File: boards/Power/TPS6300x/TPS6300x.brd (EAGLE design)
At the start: 26.7 x 10.2 mm, 9 parts

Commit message: Minor edits to the TPS6300x board and its library footprint
- Added external enable pin (might want this for APRS 3.3v)
- Fixed text issues with the footprint (didn't add EN yet)
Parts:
- added EXT_EN: M01PTH, SparkFun-Connectors:1X01
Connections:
- net EN: now also EXT_EN.1
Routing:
- net EN: track 20.1 -> 25.0 mm
- net 1.8V: track 30.7 -> 32.2 mm
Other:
- board text added: "EN"
- board text added: "v2"
- board text removed: "v1"
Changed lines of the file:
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@@
 <wire x1="26.67" y1="10.16" x2="0" y2="10.16" width="0" layer="20"/>
 <wire x1="0" y1="10.16" x2="0" y2="0" width="0" layer="20"/>
-<text x="23.495" y="0.635" size="1.778" layer="21">-</text>
 <text x="23.495" y="7.62" size="1.778" layer="21">+</text>
 <text x="8.255" y="7.62" size="1.778" layer="21">+</text>
 <text x="9.525" y="7.62" size="1.778" layer="22" rot="MR0">+</text>
 <text x="24.765" y="7.62" size="1.778" layer="22" rot="MR0">+</text>
-<text x="24.765" y="0.635" size="1.778" layer="22" rot="MR0">-</text>
 <text x="9.525" y="0.635" size="1.778" layer="22" rot="MR0">-</text>
-<text x="10.16" y="1.905" size="1.6764" layer="22" rot="MR180">TPS6300x</text>
-<text x="0" y="1.905" size="1.6764" layer="22" rot="MR180">v1</text>
+<text x="10.541" y="9.779" size="1.6764" layer="22" rot="MR180">TPS6300x</text>
+<text x="10.541" y="7.239" size="1.6764" layer="22" rot="MR180">v2</text>
+<text x="22.86" y="1.905" size="1.27" layer="25" rot="R180">EN</text>
 </plain>
 <attributes>
@@
 <attribute name="VALUE" x="3.81" y="0.127" size="0.4064" layer="27"/>
 </element>
+<element name="EXT_EN" library="SparkFun-Connectors" package="1X01" value="M01PTH" x="24.13" y="1.27" smashed="yes"/>
 </elements>
 <signals>
@@
 <wire x1="19.2786" y1="5.715" x2="19.5072" y2="5.4864" width="0.254" layer="1"/>
 <wire x1="19.5072" y1="5.4864" x2="20.5232" y2="4.4704" width="0.4064" layer="1"/>
-<wire x1="20.5232" y1="4.4704" x2="20.5232" y2="2.032" width="0.4064" layer="1"/>
-<wire x1="20.5232" y1="2.032" x2="19.9136" y2="1.4224" width="0.4064" layer="1"/>
-<wire x1="19.9136" y1="1.4224" x2="16.0528" y2="1.4224" width="0.4064" layer="1"/>
-<wire x1="16.0528" y1="1.4224" x2="14.9352" y2="2.54" width="0.4064" layer="1"/>
+<wire x1="20.5232" y1="4.4704" x2="20.5232" y2="3.048" width="0.4064" layer="1"/>
+<wire x1="20.5232" y1="3.048" x2="20.9296" y2="2.6416" width="0.4064" layer="1"/>
+<wire x1="20.9296" y1="2.6416" x2="20.9296" y2="1.4224" width="0.4064" layer="1"/>
+<wire x1="20.9296" y1="1.4224" x2="20.32" y2="0.8128" width="0.4064" layer="1"/>
+<wire x1="20.32" y1="0.8128" x2="16.6624" y2="0.8128" width="0.4064" layer="1"/>
+<wire x1="16.6624" y1="0.8128" x2="14.9352" y2="2.54" width="0.4064" layer="1"/>
 <wire x1="14.9352" y1="2.54" x2="14.875" y2="2.54" width="0.4064" layer="1"/>
 <wire x1="18.62" y1="5.215" x2="19.2358" y2="5.215" width="0.254" layer="1"/>
@@
 <wire x1="4.71" y1="1.27" x2="6.35" y2="1.27" width="0.254" layer="1"/>
 <via x="6.35" y="1.27" extent="1-16" drill="0.6"/>
-<wire x1="6.35" y1="1.27" x2="18.9484" y2="1.27" width="0.254" layer="16"/>
+<wire x1="6.35" y1="1.27" x2="19.1516" y2="1.27" width="0.254" layer="16"/>
 <wire x1="18.62" y1="4.715" x2="18.8562" y2="4.715" width="0.254" layer="1"/>
-<wire x1="18.8562" y1="4.715" x2="19.5072" y2="4.064" width="0.254" layer="1"/>
-<wire x1="19.5072" y1="4.064" x2="19.5072" y2="3.8608" width="0.254" layer="1"/>
-<via x="19.5072" y="3.8608" extent="1-16" drill="0.6"/>
-<wire x1="19.5072" y1="3.8608" x2="19.5072" y2="1.8288" width="0.254" layer="16"/>
-<wire x1="19.5072" y1="1.8288" x2="18.9484" y2="1.27" width="0.254" layer="16"/>
+<wire x1="18.8562" y1="4.715" x2="19.7104" y2="3.8608" width="0.254" layer="1"/>
+<wire x1="19.7104" y1="3.8608" x2="19.7104" y2="1.8288" width="0.254" layer="1"/>
+<via x="19.7104" y="1.8288" extent="1-16" drill="0.6"/>
+<wire x1="19.7104" y1="1.8288" x2="19.1516" y2="1.27" width="0.254" layer="16"/>
 <wire x1="7.99" y1="1.27" x2="6.35" y2="1.27" width="0.254" layer="1"/>
+<contactref element="EXT_EN" pad="1"/>
+<wire x1="24.13" y1="1.27" x2="20.2692" y2="1.27" width="0.254" layer="16"/>
+<wire x1="20.2692" y1="1.27" x2="19.7104" y2="1.8288" width="0.254" layer="16"/>
 </signal>
 </signals>
-<errors>
-</errors>
 </board>
 </drawing>

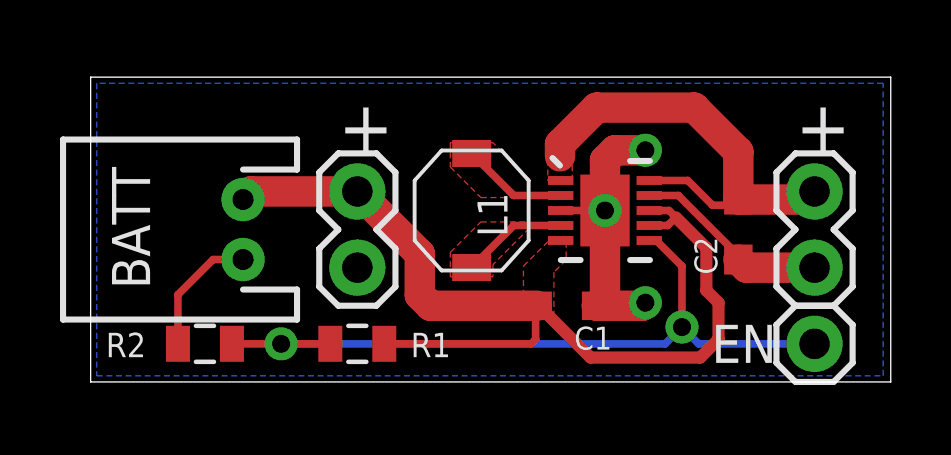
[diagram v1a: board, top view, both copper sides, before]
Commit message: TPS6300x v2
- Resistor dividor is now for the UVLO (Vina) pin, not EN
- EN is broken out so we can drive it externally
- Added SMD jumpers for UVLO and EN select
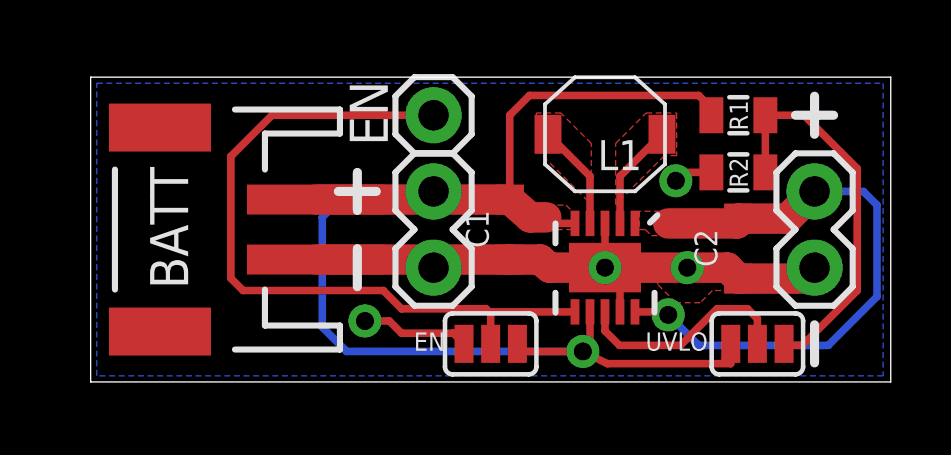
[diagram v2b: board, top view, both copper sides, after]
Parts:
- added EN_SEL: OFF/ON, SparkFun-Passives:SJ_3
- added UVLO: 1.7/2.6, SparkFun-Passives:SJ_3
- BATT_JST: device SparkFun-Connectors:JST-2-PTH -> SparkFun-Connectors:JST-2-SMD
- moved R2 18.7 mm to (21.6, 6.99)
- moved EXT_EN 14.8 mm to (11.4, 8.89)
- moved R1 14.8 mm to (21.6, 8.89), turned to 180 degrees
- moved L1 5.12 mm to (17.1, 8.26), turned to 180 degrees
- moved C1 3.17 mm to (14.0, 5.08), turned to 90 degrees
- moved BATT 2.54 mm to (11.4, 3.81)
- moved TPS63001 1.90 mm to (17.1, 3.81), turned to 180 degrees
- moved BATT_JST 1.27 mm to (3.81, 5.08)
- moved C2 0.63 mm to (21.6, 4.45)
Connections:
- new net N$4: R1.1, R2.2, UVLO.3
- new net VINA: TPS63001.8, UVLO.2
- net 1.8V: now also EN_SEL.1, UVLO.1; no longer TPS63001.8
- net EN: now also EN_SEL.2; no longer R1.1, R2.2
- net GND: now also EN_SEL.3
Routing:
- net 1.8V: track 32.2 -> 45.5 mm, vias 0 -> 1
- net N$4: track 0.00 -> 13.0 mm
- net VINA: track 0.00 -> 7.39 mm
- net GND: track 26.9 -> 31.9 mm, vias 3 -> 4
- net 3.3V: track 15.1 -> 19.9 mm, vias 0 -> 1
- net EN: track 25.0 -> 24.4 mm, vias 2 -> 0
- added copper zone on layer 1, net GND
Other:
- board text removed: "+"
- board text removed: "-"
